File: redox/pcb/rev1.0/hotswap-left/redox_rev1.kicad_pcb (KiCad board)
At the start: 2 copper layers, 162.2 x 126.5 mm, 83 parts, among them K0 KEYSW, K1 KEYSW, K10 KEYSW, K11 KEYSW, K12 KEYSW, K13 KEYSW, K14 KEYSW, K15 KEYSW, K16 KEYSW, K2 KEYSW, K20 KEYSW, K21 KEYSW, K22 KEYSW, K23 KEYSW, K24 KEYSW, K25 KEYSW, K26 KEYSW, K3 KEYSW, K30 KEYSW, K31 KEYSW, K32 KEYSW, K33 KEYSW, K34 KEYSW, K35 KEYSW, K36 KEYSW, K4 KEYSW, K40 KEYSW, K41 KEYSW, K42 KEYSW, K43 KEYSW, K44 KEYSW, K45 KEYSW, K46 KEYSW, K5 KEYSW, K6 KEYSW, U1 ProMicro

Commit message: Route more nets
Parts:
- removed RGB_STRIP1: Conn_01x03, Pin_Headers:Pin_Header_Straight_1x03_Pitch2.54mm
- moved D42 1.27 mm to (144.6, 141.0)
- turned K16 to 0 degrees
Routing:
- net row3: track 0.00 -> 151.7 mm
- net row4: track 0.00 -> 120.2 mm
- net col5: track 30.1 -> 130.1 mm
- net col6: track 59.1 -> 158.7 mm
- net col3: track 0.00 -> 94.2 mm
- net row2: track 119.3 -> 184.5 mm, vias 2 -> 1
- net col4: track 0.00 -> 61.4 mm
- net row1: track 169.3 -> 118.1 mm, vias 1 -> 0
- net VCC: track 62.5 -> 16.0 mm, vias 2 -> 0
- net Net-(D35-Pad2): track 0.00 -> 16.9 mm
- net Net-(D15-Pad2): track 0.00 -> 16.9 mm
- net Net-(D26-Pad2): track 0.00 -> 16.4 mm
- net Net-(D5-Pad2): track 0.00 -> 16.1 mm
- net Net-(D25-Pad2): track 0.00 -> 16.1 mm
- net Net-(D16-Pad2): track 0.00 -> 16.1 mm
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
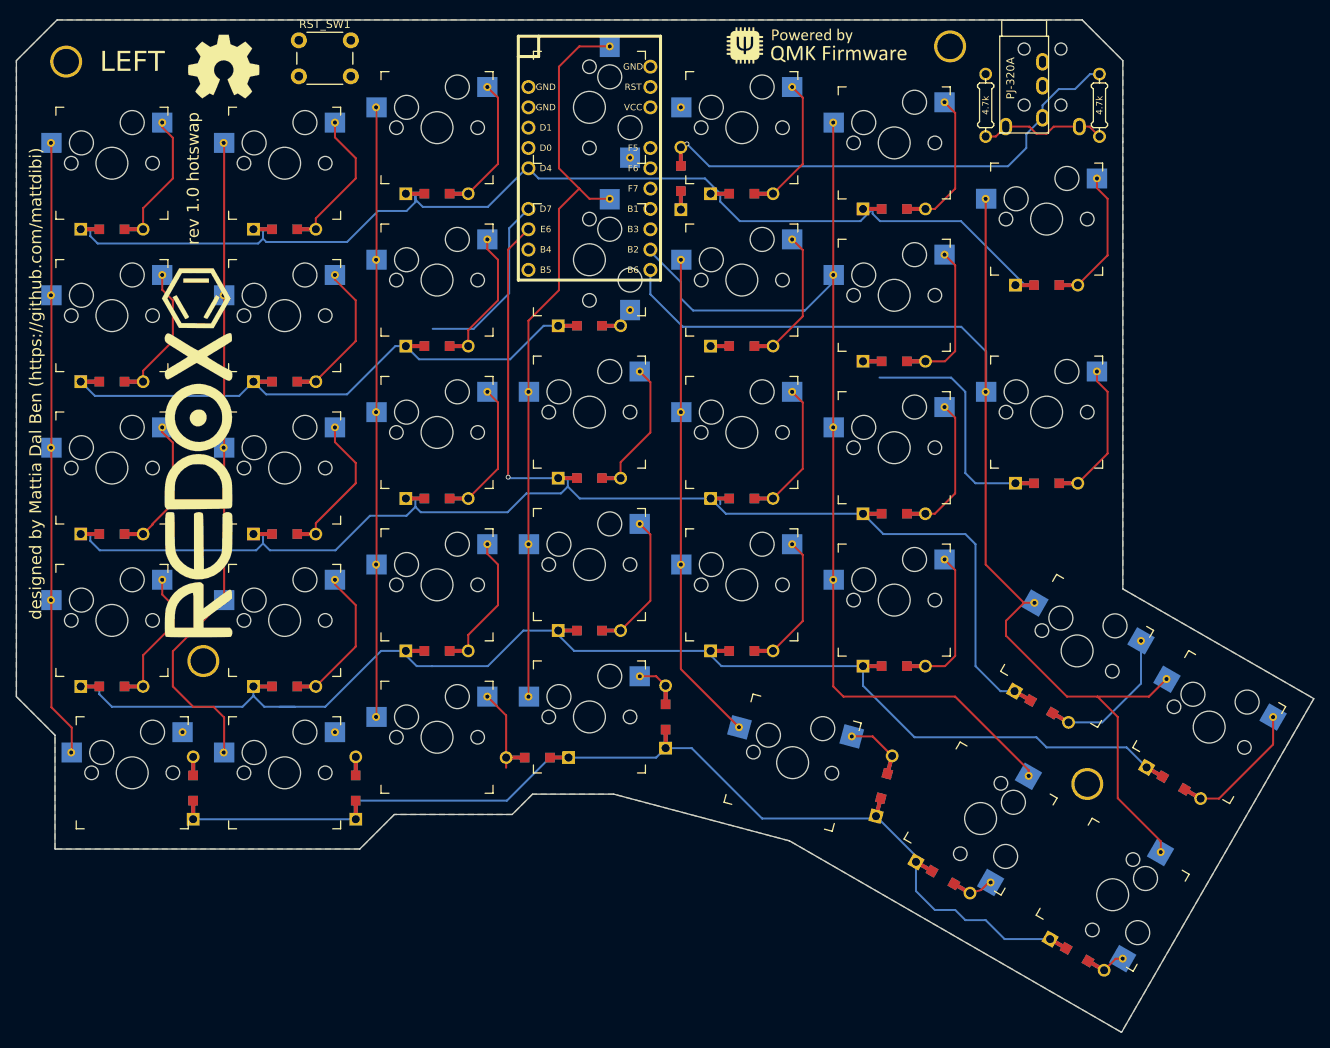
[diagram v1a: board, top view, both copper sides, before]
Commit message: Complete left PCB
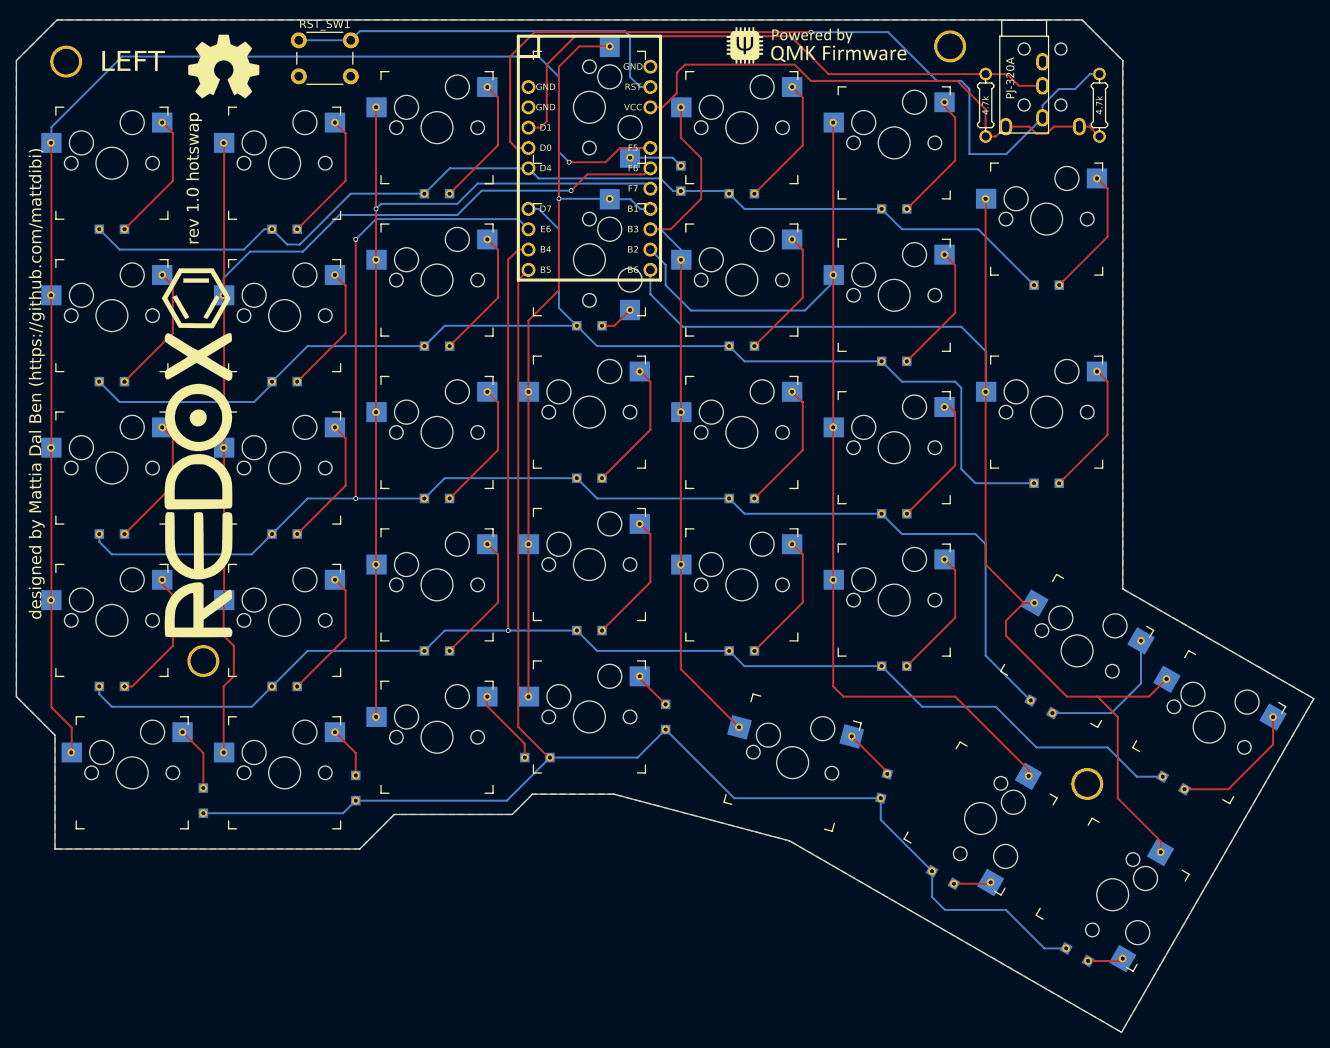
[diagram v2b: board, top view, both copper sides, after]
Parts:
- D0, D1, D10, D11, D12, D13, D14, D15, D16, D2, D20, D21, D22, D23, D24, D25, D26, D3, D30, D31, D32, D33, D34, D35, D36, D4, D40, D41, D42, D43, D44, D45, D46, D5, D6: footprint redox_footprints:Diode-dual -> redox_footprints:Diode-smd-via
- moved D40 2.02 mm to (102.9, 146.4)
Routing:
- net col0: track 77.3 -> 169.5 mm, vias 0 -> 1
- net SDA: track 0.00 -> 75.7 mm
- net row4: track 120.2 -> 190.2 mm
- net col1: track 83.0 -> 138.4 mm, vias 0 -> 1
- net VCC: track 16.0 -> 67.3 mm
- net RST: track 0.00 -> 50.3 mm
- net SCL: track 59.4 -> 104.3 mm
- net row3: track 151.7 -> 195.5 mm, vias 0 -> 1
- net row1: track 118.1 -> 154.4 mm
- net col2: track 76.2 -> 112.0 mm, vias 0 -> 1
- net col4: track 61.4 -> 88.0 mm
- net row2: track 184.5 -> 197.2 mm, vias 1 -> 2
- net Net-(D40-Pad2): track 0.00 -> 8.06 mm
- net Net-(D3-Pad2): track 0.00 -> 6.77 mm
- net Net-(D41-Pad2): track 0.00 -> 6.49 mm
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
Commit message: Add 3D models to left PCB
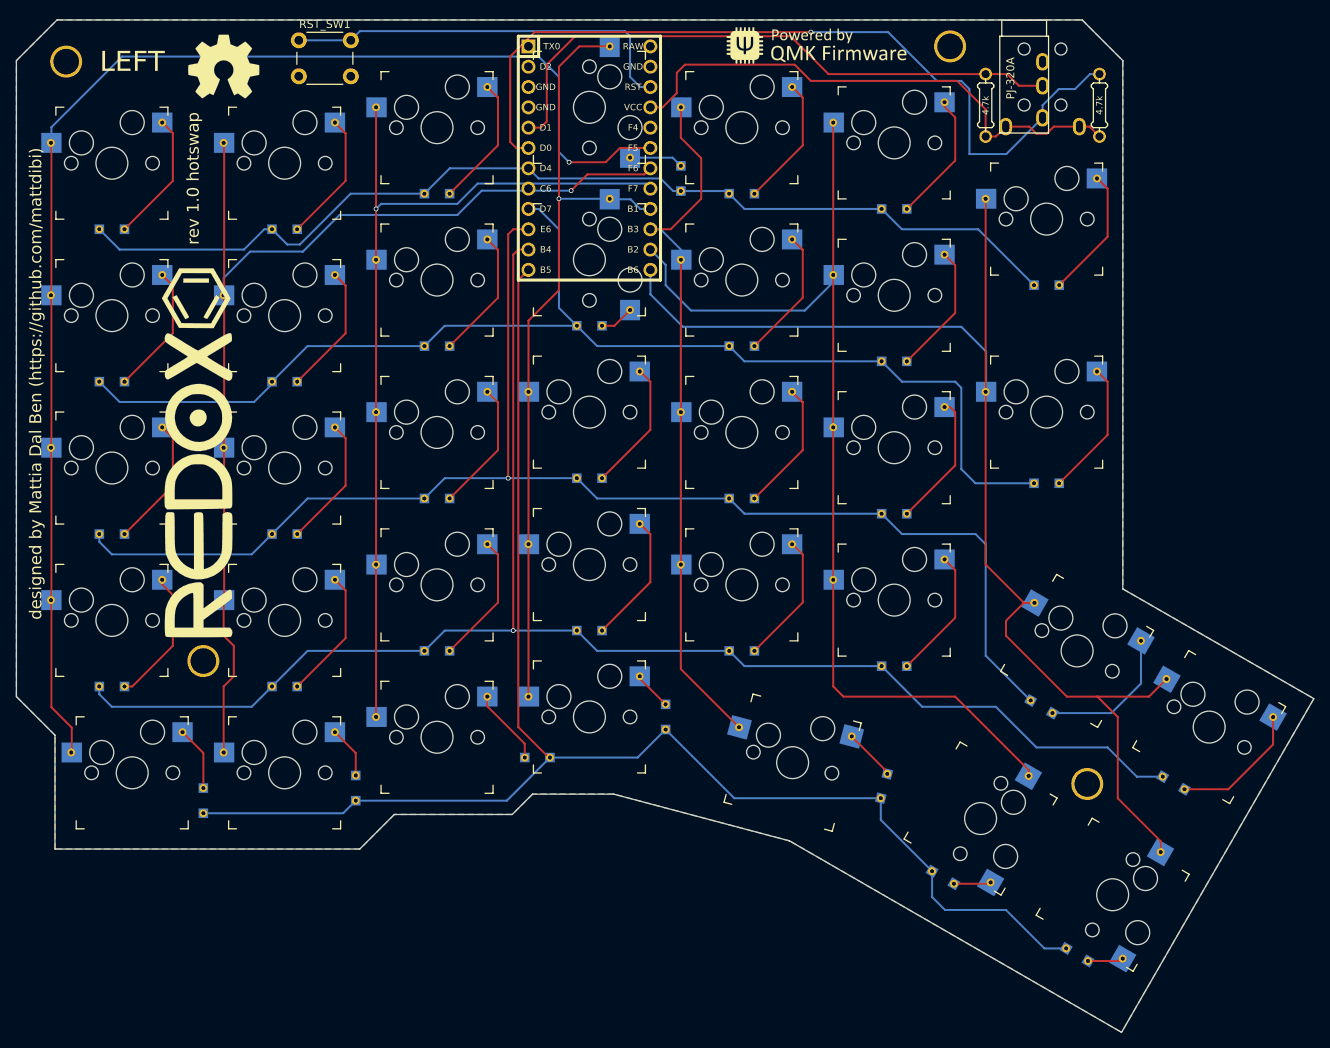
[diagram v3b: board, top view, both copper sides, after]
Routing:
- net row2: track 197.2 -> 175.0 mm, vias 2 -> 1
